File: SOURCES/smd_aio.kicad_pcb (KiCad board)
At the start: 2 copper layers, 434 parts, among them J1 RCA_01, J2 RCA_01, J3 RCA_01, J4 RCA_01, P1 CONN_01X06, P10 CONN_01X02, P11 FCR684205T, P12 FCR684205R, P13 CONN_01X02, P14 CONN_01X02, P15 CONN_01X02, P16 TST, P17 TST, P18 TST, P19 TST, P2 CONN_01X04, P20 TST, P21 TST, P22 TST, P23 TST, P24 TST, P25 TST, P26 TST, P27 TST, P28 TST, P29 TST, P3 CONN_01X03, P30 TST, P31 CONN_01X03, P4 CONN_02X05 Boxed, P5 STDCONN, P6 CONN_02X04, P7 CONN_02X04, P8 CONN_02X04, P9 CONN_01X02, Q1 BSS123, Q2 BSS123, Q3 BSS123, Q4 BSS123, Q5 FZT751TA, SW1 SW_PUSH, T1 Transformer_1P_1S_DA101JC, T2 Transformer_1P_1S_DA101JC, U1 ADAU1701, U10 IDT2309NZ, U2 24AA256SN, U3 SN74LVC14ADG4, U4 TAS5760MDCAR, U5 CS8422-CNZ, U6 CS8406-CZZ, U7 LM2842Y, U8 SN74LVC14ADG4, U9 TAS5760MDCAR, X1 ASV-24.576MHz-EJ-T

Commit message: Converted to KiCad7
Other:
- net class +3V3 removed
- net class ADAU removed
- net class Default removed
- net class Default AMP removed
- net class VCC removed

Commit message: DRC checked.
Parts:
- removed ? (x3), REF**: MountingHole_3.2mm_M3_DIN965, fdsp_drillhole:MountingHole_3.2mm_M3_DIN965
- removed ? (x209): , AMPx2 _footprints:Via
- removed ? (x3): FIDUCIAL_1MM_DOT, fdsp_fiducial:FIDUCIAL_1MM_DOT
- removed G*** (x2): LOGO, fdsp_misc:LOGO_FREEDSP_600dpi
- removed P25: TST, fdsp_misc:Measurement_Point_Round-SMD-Pad_Small
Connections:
- P4 pad 2: Net-(P4-Pad2) -> unconnected-(P4-P2-Pad2)
- P4 pad 5: Net-(P4-Pad5) -> unconnected-(P4-P5-Pad5)
- P4 pad 7: Net-(P4-Pad7) -> unconnected-(P4-P7-Pad7)
- P4 pad 8: Net-(P4-Pad8) -> unconnected-(P4-P8-Pad8)
- P4 pad 9: Net-(P4-Pad9) -> unconnected-(P4-P9-Pad9)
- T1 pad 2: Net-(T1-Pad2) -> unconnected-(T1-NC-Pad2)
- T1 pad 5: Net-(T1-Pad5) -> unconnected-(T1-NC-Pad5)
- T2 pad 2: Net-(T2-Pad2) -> unconnected-(T2-NC-Pad2)
- T2 pad 5: Net-(T2-Pad5) -> unconnected-(T2-NC-Pad5)
- U1 pad 20: Net-(U1-Pad20) -> unconnected-(U1-ADDR1/CDATA/WB-Pad20)
- U1 pad 31: Net-(U1-Pad31) -> unconnected-(U1-OSCO-Pad31)
- U3 pad 10: Net-(U3-Pad10) -> unconnected-(U3-5Y-Pad10)
- U3 pad 12: Net-(U3-Pad12) -> unconnected-(U3-6Y-Pad12)
- U3 pad 8: Net-(U3-Pad8) -> unconnected-(U3-4Y-Pad8)
- U4 pad 18: Net-(U4-Pad18) -> unconnected-(U4-Pad18)
- U4 pad 19: Net-(U4-Pad19) -> unconnected-(U4-Pad19)
- U4 pad 20: Net-(U4-Pad20) -> unconnected-(U4-Pad20)
- U4 pad 21: Net-(U4-Pad21) -> unconnected-(U4-Pad21)
- U4 pad 22: Net-(U4-Pad22) -> unconnected-(U4-Pad22)
- U4 pad 23: Net-(U4-Pad23) -> unconnected-(U4-Pad23)
- U4 pad 24: Net-(U4-Pad24) -> unconnected-(U4-Pad24)
- U4 pad 25: Net-(U4-Pad25) -> unconnected-(U4-Pad25)
- U4 pad 26: Net-(U4-Pad26) -> unconnected-(U4-Pad26)
- U4 pad 27: Net-(U4-Pad27) -> unconnected-(U4-Pad27)
- U4 pad 28: Net-(U4-Pad28) -> unconnected-(U4-Pad28)
- U4 pad 29: Net-(U4-Pad29) -> unconnected-(U4-Pad29)
- U4 pad 30: Net-(U4-Pad30) -> unconnected-(U4-Pad30)
- U4 pad 31: Net-(U4-Pad31) -> unconnected-(U4-Pad31)
- U5 pad 10: Net-(U5-Pad10) -> unconnected-(U5-V/*AUDIO-Pad10)
- U5 pad 12: Net-(U5-Pad12) -> unconnected-(U5-XTO-Pad12)
- U5 pad 16: Net-(U5-Pad16) -> unconnected-(U5-RCBL-Pad16)
- U5 pad 18: Net-(U5-Pad18) -> unconnected-(U5-TX/U-Pad18)
- U5 pad 23: Net-(U5-Pad23) -> unconnected-(U5-SDOUT2-Pad23)
- U5 pad 24: Net-(U5-Pad24) -> unconnected-(U5-OSCLK2-Pad24)
- U5 pad 25: Net-(U5-Pad25) -> unconnected-(U5-OLRCK2-Pad25)
- U5 pad 31: Net-(U5-Pad31) -> unconnected-(U5-RMCK-Pad31)
- U8 pad 10: Net-(U8-Pad10) -> unconnected-(U8-5Y-Pad10)
- U8 pad 12: Net-(U8-Pad12) -> unconnected-(U8-6Y-Pad12)
- U8 pad 8: Net-(U8-Pad8) -> unconnected-(U8-4Y-Pad8)
- U9 pad 18: Net-(U9-Pad18) -> unconnected-(U9-Pad18)
- U9 pad 19: Net-(U9-Pad19) -> unconnected-(U9-Pad19)
- U9 pad 20: Net-(U9-Pad20) -> unconnected-(U9-Pad20)
- U9 pad 21: Net-(U9-Pad21) -> unconnected-(U9-Pad21)
- U9 pad 22: Net-(U9-Pad22) -> unconnected-(U9-Pad22)
- U9 pad 23: Net-(U9-Pad23) -> unconnected-(U9-Pad23)
- U9 pad 24: Net-(U9-Pad24) -> unconnected-(U9-Pad24)
- U9 pad 25: Net-(U9-Pad25) -> unconnected-(U9-Pad25)
- U9 pad 26: Net-(U9-Pad26) -> unconnected-(U9-Pad26)
- U9 pad 27: Net-(U9-Pad27) -> unconnected-(U9-Pad27)
- U9 pad 28: Net-(U9-Pad28) -> unconnected-(U9-Pad28)
- U9 pad 29: Net-(U9-Pad29) -> unconnected-(U9-Pad29)
- U9 pad 30: Net-(U9-Pad30) -> unconnected-(U9-Pad30)
- U9 pad 31: Net-(U9-Pad31) -> unconnected-(U9-Pad31)
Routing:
- net GND: track 152.7 -> 150.6 mm, vias 15 -> 26
- net VCC: track 294.9 -> 296.1 mm
- net MP10: track 264.5 -> 263.7 mm
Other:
- board outline added: 159.8 x 99.8 mm

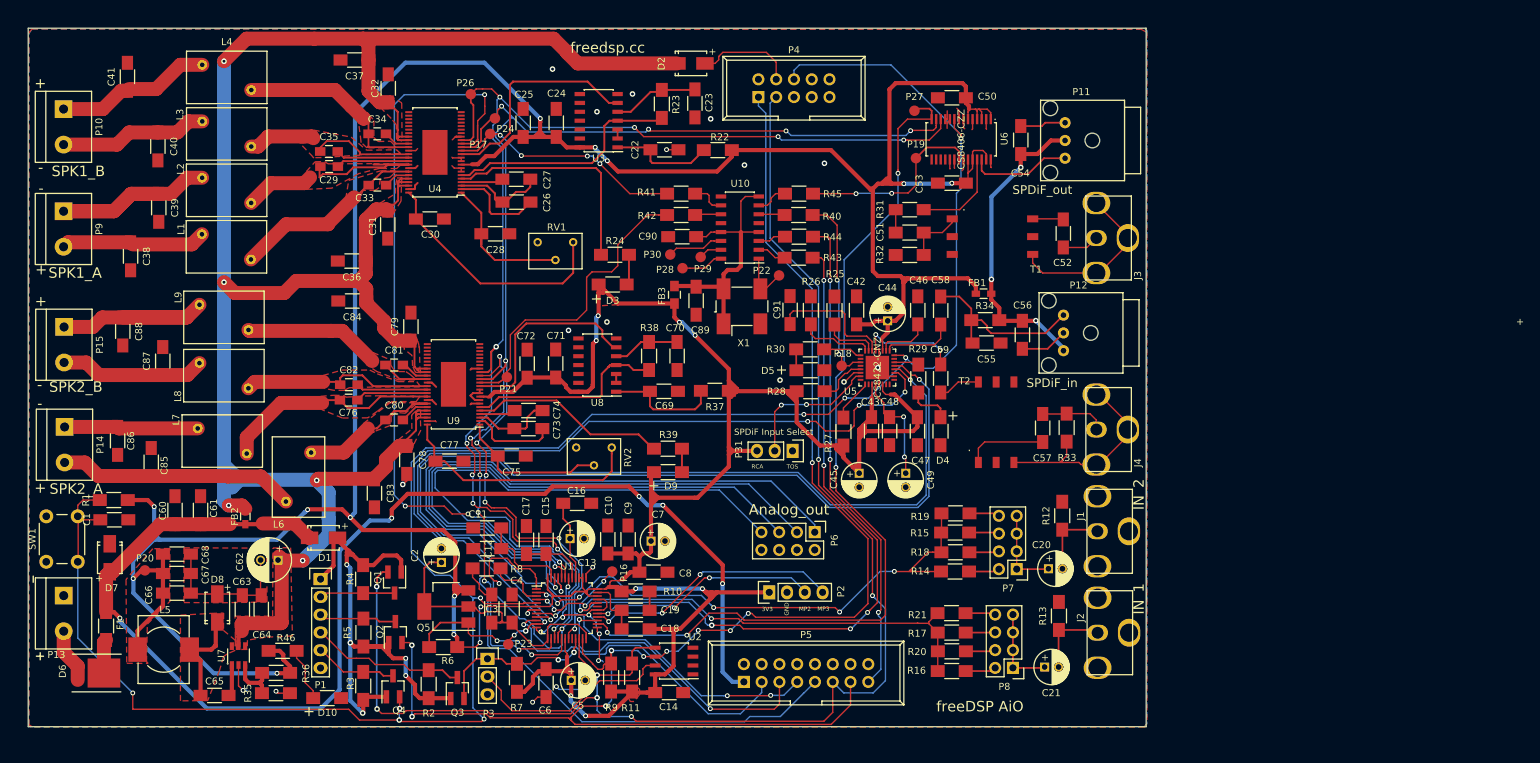
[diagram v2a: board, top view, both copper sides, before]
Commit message: Removed redundant 7414 and pot, rerouted a bit.
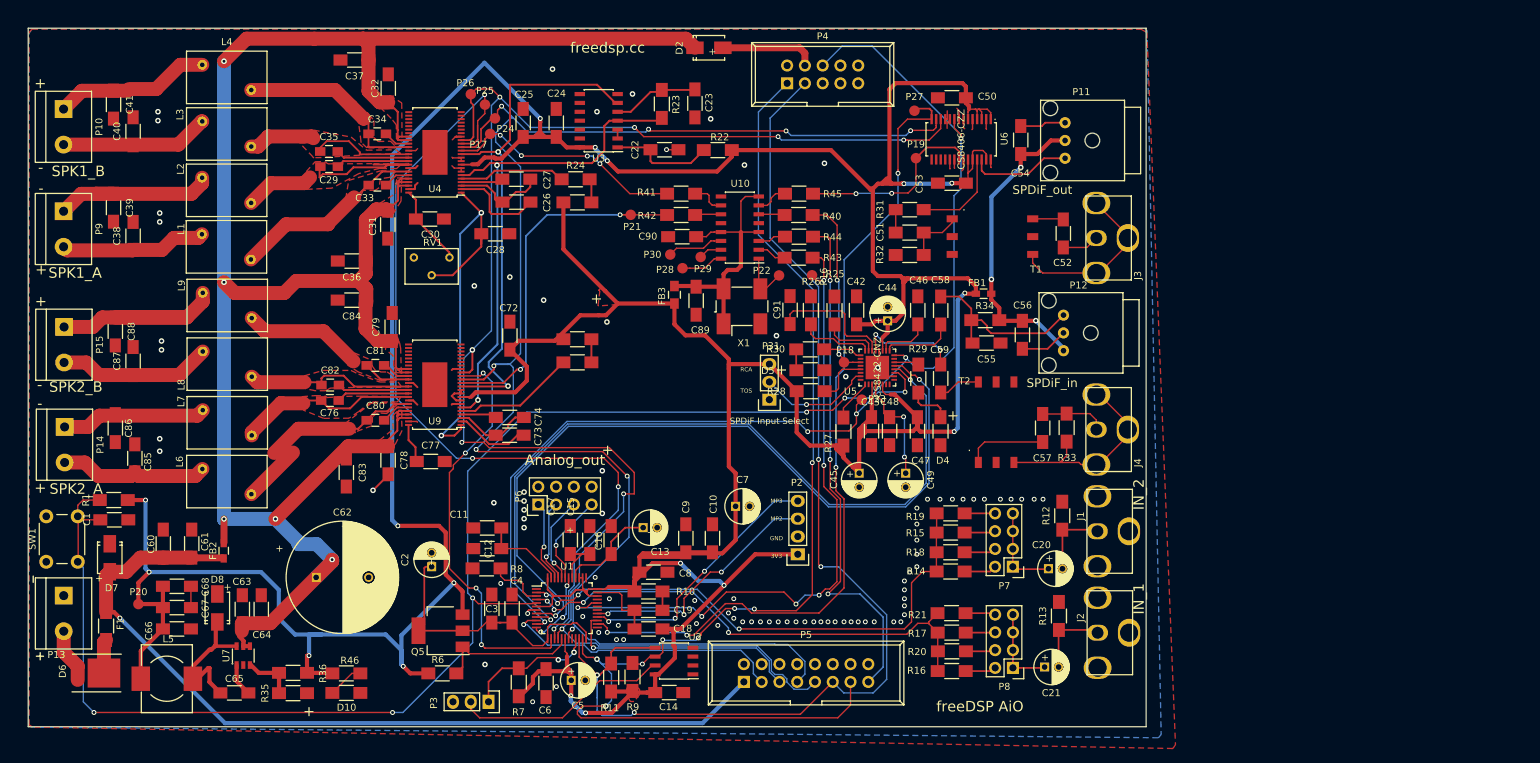
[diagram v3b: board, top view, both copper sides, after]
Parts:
- removed C69, C70, C75: 1u/16V, fdsp_capacitor:C_1206_HandSoldering
- removed C71: 0u1/50V, fdsp_capacitor:C_1206_HandSoldering
- removed D1: B150, fdsp_diode:SMA
- removed P1: CONN_01X06, fdsp_pinheader:Pin_Header_Straight_1x06
- removed Q1, Q2, Q3, Q4: BSS123, fdsp_housing_new:SOT-23_Handsoldering
- removed R2, R3, R4, R5: 10K, fdsp_resistor:R_1206_HandSoldering
- removed R37, R38: 100k, fdsp_resistor:R_1206_HandSoldering
- removed RV2: 100k, AMPx2 _footprints:M64Z104KB40
- removed U8: SN74LVC14ADG4, Housings_SOIC:SOIC-14_3.9x8.7mm_Pitch1.27mm
- added P25: TST, fdsp_misc:Measurement_Point_Round-SMD-Pad_Small, F.Cu at (84.1, 27.9)
- C62: footprint fdsp_capacitor:C_Radial_D6.3_L11.2_P2.5 -> fdsp_capacitor:C_Radial_D16_L25_P7.5
- moved P23 61.4 mm to (137.9, 70.1)
- moved P16 51.1 mm to (130.8, 52.3)
- moved P6 39.7 mm to (91.7, 85.1), turned to 90 degrees
- moved P21 29.2 mm to (104.9, 43.7)
- moved D9 23.0 mm to (97.3, 61.5)
- moved R39 17.9 mm to (97.3, 64.8)
- moved RV1 17.8 mm to (76.5, 52.3)
- moved C10 15.0 mm to (116.6, 89.9)
- moved C7 13.1 mm to (119.9, 85.3)
- moved D3 12.8 mm to (97.3, 41.9)
- moved R24 12.2 mm to (97.0, 38.6)
- moved C13 10.6 mm to (106.7, 88.4)
- moved L6 10.3 mm to (47.2, 81.8), turned to 180 degrees
- moved R46 9.66 mm to (64.3, 109.2)
- moved C9 8.25 mm to (112.8, 89.9)
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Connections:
- net Net-(U7-FB) renamed /Power/lm-fb
- C28 pad 2: Net-(U4-SFT_CLIP) -> SFT_CLIP
- R23 pad 1: Net-(U3-2Y) -> SPK_SD
- RV1 pad 2: Net-(U4-SFT_CLIP) -> SFT_CLIP
- U3 pad 4: Net-(U3-2Y) -> SPK_SD
- U3 pad 6: Net-(U3-3Y) -> SPK_SLEEP
- U4 pad 1: Net-(U4-SFT_CLIP) -> SFT_CLIP
- U4 pad 12: Net-(U3-3Y) -> SPK_SLEEP
- U4 pad 6: Net-(U3-2Y) -> SPK_SD
- U9 pad 1: Net-(U9-SFT_CLIP) -> SFT_CLIP
- U9 pad 12: Net-(U8-3Y) -> SPK_SLEEP
- U9 pad 6: Net-(U8-2Y) -> SPK_SD
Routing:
- net VOUT0: track 92.4 -> 11.8 mm
- net VOUT1: track 89.8 -> 11.8 mm
- net +5V: track 76.8 -> 0.00 mm, vias 5 -> 0
- net SPK_SLEEP: track 0.00 -> 74.6 mm, vias 0 -> 2
- net GND: track 150.6 -> 76.9 mm, vias 26 -> 94
- net SPK_SD: track 0.00 -> 71.7 mm, vias 0 -> 2
- net VOUT2: track 82.5 -> 12.4 mm
- net VOUT3: track 77.4 -> 13.1 mm
- net VIN: track 180.8 -> 123.3 mm, vias 5 -> 1
- net SFT_CLIP: track 0.00 -> 57.1 mm, vias 0 -> 2
- net SDA: track 215.4 -> 163.2 mm, vias 7 -> 4
- net SCL: track 223.6 -> 177.2 mm, vias 10 -> 8
- net Net-(U3-2Y): track 34.1 -> 0.00 mm
- net Net-(U3-3Y): track 32.0 -> 0.00 mm
- net Net-(U9-GVDD_REG): track 36.0 -> 5.71 mm
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- removed copper zone on F.Cu, net Net-(D8-K)

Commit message: Removed ArduinoPort, Changed Power Supply. Rerouting and stuff.
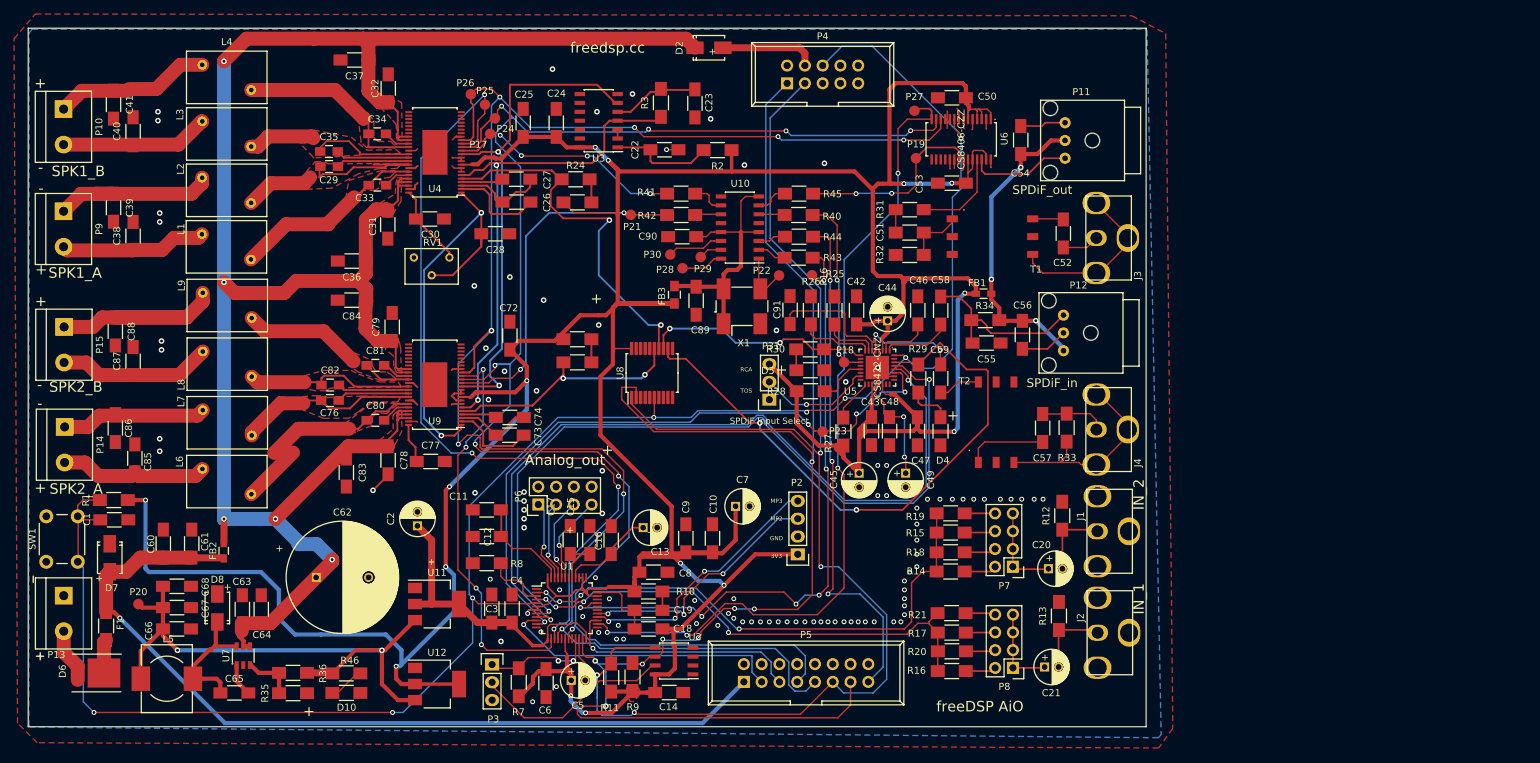
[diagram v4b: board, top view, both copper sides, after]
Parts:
- removed Q5: FZT751TA, fdsp_housing_new:SOT-223
- removed R22, R23: 100k, fdsp_resistor:R_1206_HandSoldering
- removed R6: 1K 1%, fdsp_resistor:R_1206_HandSoldering
- added R2: 100k, fdsp_resistor:R_1206_HandSoldering, F.Cu at (117.3, 34.4)
- added R3: 100k, fdsp_resistor:R_1206_HandSoldering, F.Cu at (109.2, 27.7)
- added U11: LM1117MP-1.8, Package_TO_SOT_SMD:SOT-223-3_TabPin2, F.Cu at (77.2, 99.3)
- added U12: LM1117MP-3.3, Package_TO_SOT_SMD:SOT-223-3_TabPin2, F.Cu at (77.2, 110.7)
- added U8: MCP23008-xSS, Package_SO:SSOP-20_5.3x7.2mm_P0.65mm, F.Cu at (108.0, 66.3)
- R46: value 330 -> 1k
- moved P23 7.22 mm to (132.3, 74.7)
- moved C2 6.19 mm to (74.4, 88.1)
- moved P3 5.36 mm to (85.1, 108.0), turned to 0 degrees
- moved C11 2.59 mm to (84.3, 85.9)
- moved C12 1.73 mm to (84.3, 89.7)
- moved R8 0.74 mm to (84.3, 93.5)
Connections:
- net Net-(P31-P2) renamed RX_SEL
- net Net-(Q5-C) renamed +1V8
- net Net-(U4-!SPK_FAULT) renamed SPK_FAULT1
- net Net-(U5-NV/RERR) renamed NV_RERR
- net Net-(U5-SRC_UNLOCK) renamed SRC_UNLOCK
- net Net-(U9-!SPK_FAULT) renamed SPK_FAULT2
- C66 pad 1: +3V3 -> +6V
- C67 pad 1: +3V3 -> +6V
- C68 pad 1: +3V3 -> +6V
- L5 pad 2: +3V3 -> +6V
- P20 pad 1: +3V3 -> +6V
- R36 pad 1: +3V3 -> +6V
- R46 pad 1: +3V3 -> +6V
- U1 pad 17: Net-(Q5-B) -> GND
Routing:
- net +3V3: track 744.8 -> 659.2 mm, vias 17 -> 15
- net SRC_UNLOCK: track 3.58 -> 86.7 mm, vias 0 -> 2
- net +6V: track 0.00 -> 79.9 mm, vias 0 -> 2
- net SPK_FAULT1: track 15.3 -> 52.9 mm, vias 0 -> 2
- net SCL: track 177.2 -> 212.7 mm
- net SDA: track 163.2 -> 194.2 mm
- net NV_RERR: track 6.05 -> 33.0 mm, vias 0 -> 2
- net Net-(Q5-B): track 20.1 -> 0.00 mm
- net SPK_FAULT2: track 17.5 -> 35.3 mm, vias 0 -> 2
- net GND: track 76.9 -> 62.2 mm, vias 94 -> 101
- net MP10: track 233.8 -> 238.8 mm
- net MP6: track 122.2 -> 118.8 mm
- net WP: track 19.2 -> 16.2 mm
- net +1V8: track 40.7 -> 43.1 mm
- net MP5: track 111.4 -> 113.6 mm
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
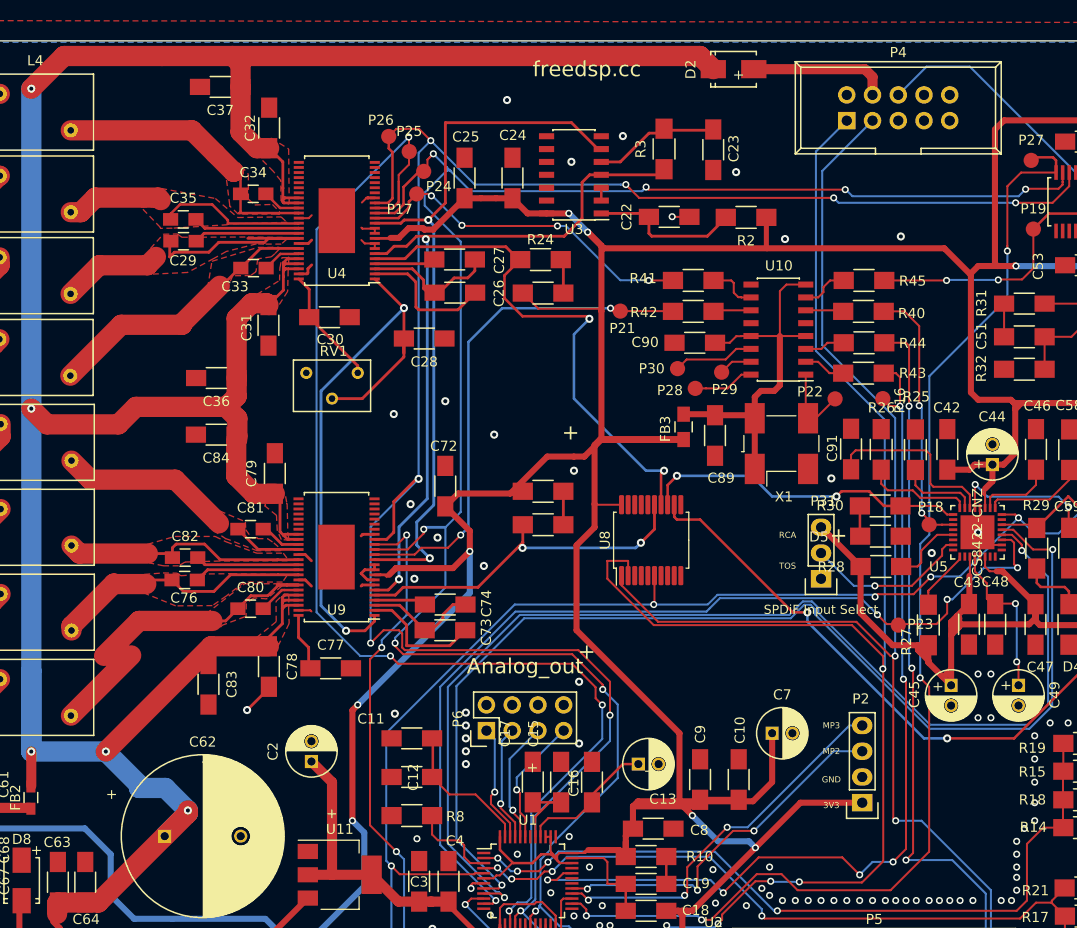
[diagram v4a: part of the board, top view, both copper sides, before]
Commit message: Added power down detection.
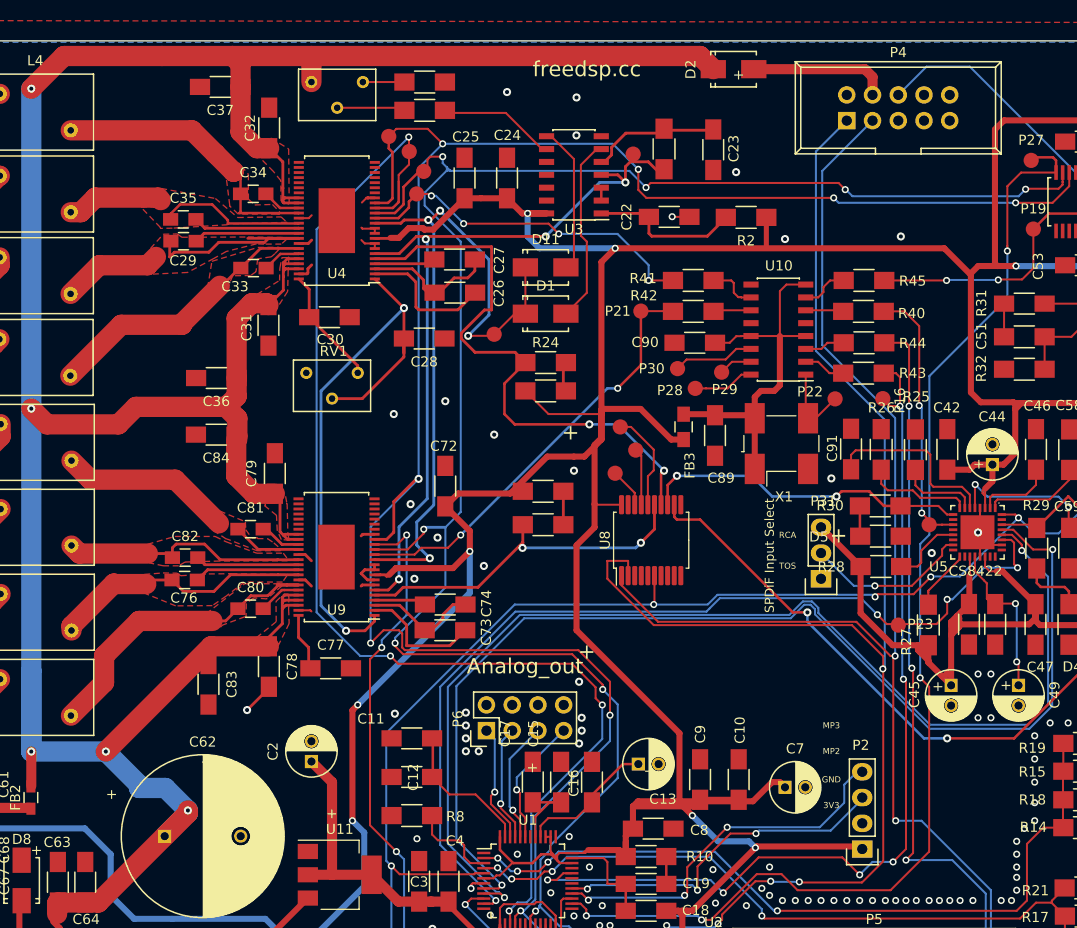
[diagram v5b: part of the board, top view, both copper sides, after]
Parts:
- added D1: B150, fdsp_diode:SMA, F.Cu at (97.5, 43.9)
- added D11: B150, fdsp_diode:SMA, F.Cu at (97.5, 39.4)
- added P1: MUTE, fdsp_misc:Measurement_Point_Round-SMD-Pad_Small, F.Cu at (92.5, 46.0)
- added P32: /SD, fdsp_misc:Measurement_Point_Round-SMD-Pad_Small, F.Cu at (106.2, 28.2)
- added P33: GP4, fdsp_misc:Measurement_Point_Round-SMD-Pad_Small, F.Cu at (104.9, 55.1)
- added P34: GP5, fdsp_misc:Measurement_Point_Round-SMD-Pad_Small, F.Cu at (106.4, 57.4)
- added P35: GP6, fdsp_misc:Measurement_Point_Round-SMD-Pad_Small, F.Cu at (104.4, 59.7)
- added R4: 10K, fdsp_resistor:R_1206_HandSoldering, F.Cu at (85.6, 21.1)
- added R5: 10K, fdsp_resistor:R_1206_HandSoldering, F.Cu at (85.6, 23.9)
- added RV2: 100k, AMPx2 _footprints:M64Z104KB40, F.Cu at (77.0, 23.6)
- P17: value TST -> MC4
- P24: value TST -> MP11
- P25: value TST -> MP6
- P26: value TST -> MP10
- U5: value CS8422-CNZ -> CS8422
- U8: value MCP23008-xSS -> MCP23008
- moved R24 10.2 mm to (97.5, 48.8)
- moved D3 9.66 mm to (97.5, 51.6)
- moved C7 5.48 mm to (121.2, 90.7)
- moved P2 4.57 mm to (128.8, 96.8)
- moved P21 2.03 mm to (106.9, 43.7)
- moved C24 0.53 mm to (93.7, 30.6)
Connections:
- U3 pad 6: SPK_SLEEP -> Net-(D1-A)
- U3 pad 8: unconnected-(U3-4Y-Pad8) -> Net-(D11-A)
- U3 pad 9: GND -> Net-(U3-4A)
- U8 pad 16: unconnected-(U8-GP4-Pad16) -> Net-(U8-GP4)
- U8 pad 17: unconnected-(U8-GP5-Pad17) -> Net-(U8-GP5)
- U8 pad 18: unconnected-(U8-GP6-Pad18) -> Net-(U8-GP6)
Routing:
- net Net-(D1-A): track 0.00 -> 18.4 mm
- net Net-(D11-A): track 0.00 -> 14.7 mm
- net Net-(U3-4A): track 0.00 -> 11.6 mm
- net Net-(U8-GP4): track 0.00 -> 9.90 mm
- net MCLK5: track 50.4 -> 42.5 mm
- net Net-(R5-Pad2): track 0.00 -> 6.64 mm
- net +3V3: track 659.2 -> 653.6 mm
- net Net-(U8-GP5): track 0.00 -> 5.62 mm
- net SPK_FAULT1: track 52.9 -> 57.5 mm
- net Net-(R4-Pad1): track 0.00 -> 4.10 mm
- net Net-(U8-GP6): track 0.00 -> 3.90 mm
- net SPK_SD: track 71.7 -> 74.3 mm, vias 2 -> 4
- net VCC: track 302.2 -> 304.8 mm
- net MP2: track 36.1 -> 34.3 mm
- net MP10: track 238.8 -> 240.2 mm
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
